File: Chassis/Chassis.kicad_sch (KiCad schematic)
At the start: 4 parts

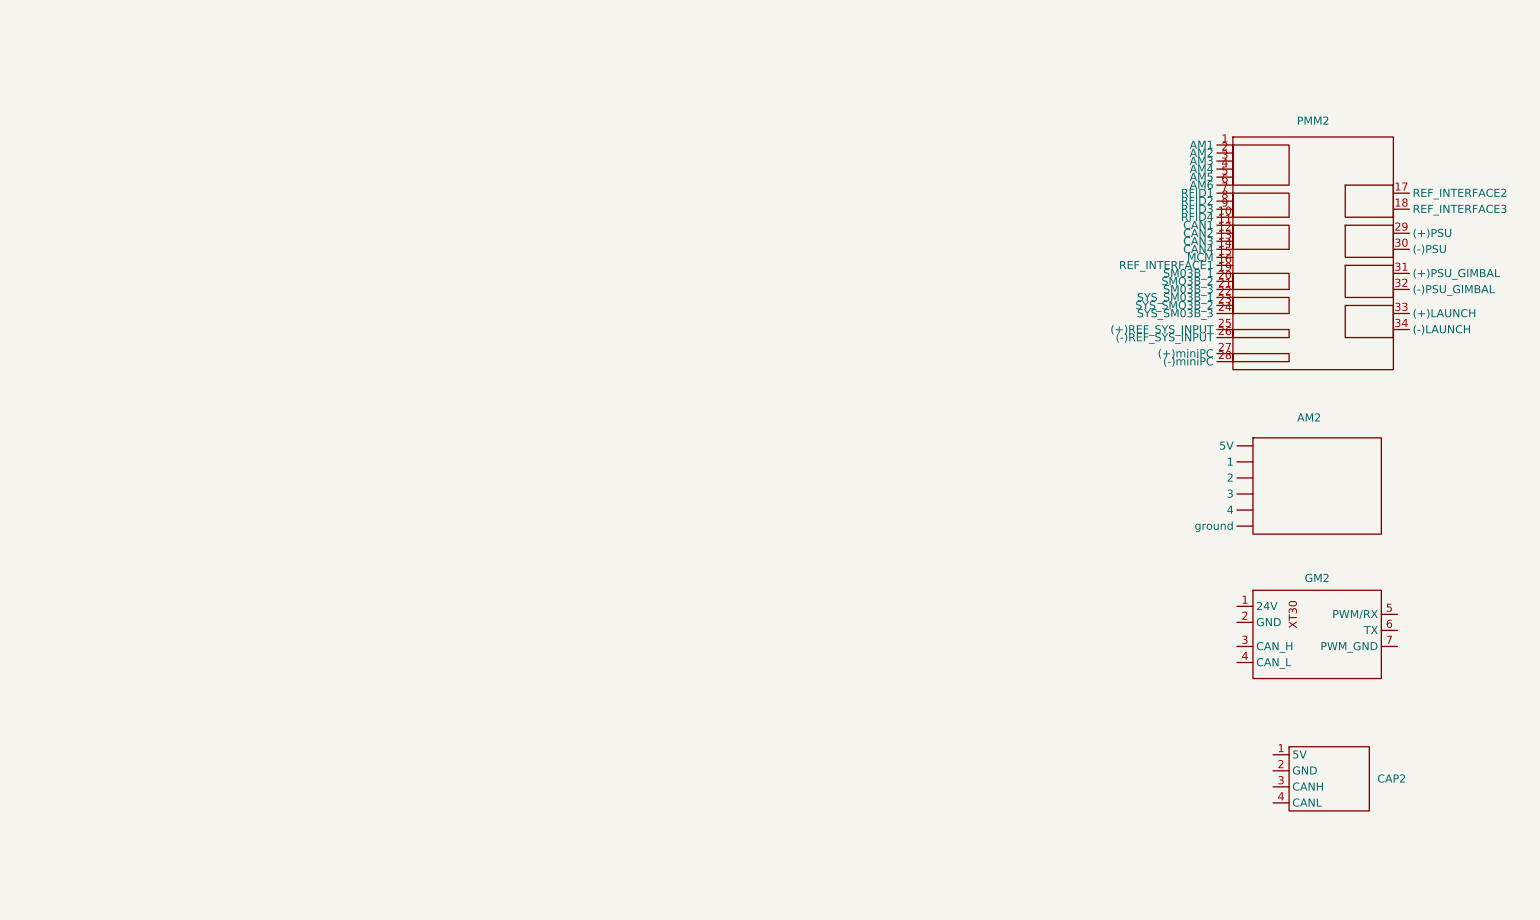
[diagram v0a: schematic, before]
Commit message: Reorganized chassis, turret, devboard shield, into monorepo
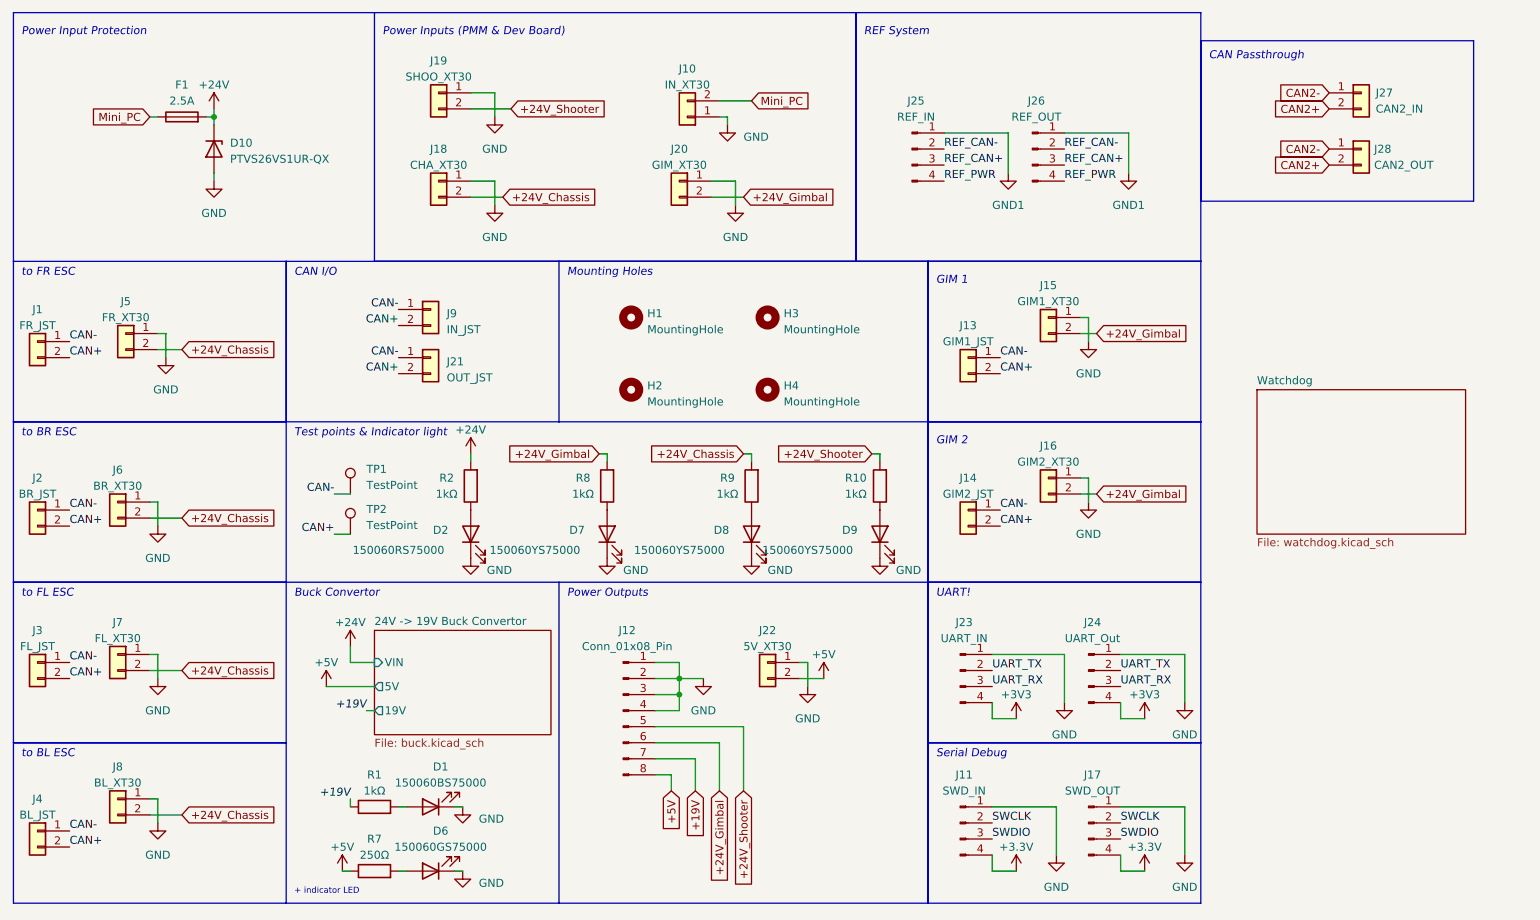
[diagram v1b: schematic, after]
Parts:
- removed AM2: ~, symbol Robomaster_Library:AM
- removed CAP2: ~, symbol Robomaster_Library:CAP
- removed GM2: ~, symbol Robomaster_Library:GM6020
- removed PMM2: ~, symbol Robomaster_Library:PMM
- added D1: 150060BS75000, LED_SMD:LED_0603_1608Metric_Pad1.05x0.95mm_HandSolder, symbol Device:LED
- added D10: PTVS26VS1UR-QX, Robomaster_Passives:PTVS26VS1URQX, symbol Device:D_Zener
- added D2: 150060RS75000, LED_SMD:LED_0603_1608Metric_Pad1.05x0.95mm_HandSolder, symbol Device:LED
- added D6: 150060GS75000, LED_SMD:LED_0603_1608Metric_Pad1.05x0.95mm_HandSolder, symbol Device:LED
- added D7, D8, D9: 150060YS75000, LED_SMD:LED_0603_1608Metric_Pad1.05x0.95mm_HandSolder, symbol Device:LED
- added F1: 2.5A, Fuse:Fuse_0603_1608Metric_Pad1.05x0.95mm_HandSolder, symbol Device:Fuse
- added H1, H2, H3, H4: MountingHole, MountingHole:MountingHole_3.2mm_M3, symbol Mechanical:MountingHole
- added J1: FR_JST, Connector_JST:JST_GH_BM02B-GHS-TBT_1x02-1MP_P1.25mm_Vertical, symbol Connector_Generic:Conn_01x02
- added J10: IN_XT30, Robomaster_Connectors:AMASS_XT30U-F_1x02_P5.0mm_Vertical, symbol Connector_Generic:Conn_01x02
- added J11: SWD_IN, Connector_JST:JST_GH_BM04B-GHS-TBT_1x04-1MP_P1.25mm_Vertical, symbol Connector:Conn_01x04_Pin
- added J12: Conn_01x08_Pin, Robomaster_Connectors:CON_1722981108_MOL, symbol Connector:Conn_01x08_Pin
- added J13: GIM1_JST, Connector_JST:JST_GH_BM02B-GHS-TBT_1x02-1MP_P1.25mm_Vertical, symbol Connector_Generic:Conn_01x02
- added J14: GIM2_JST, Connector_JST:JST_GH_BM02B-GHS-TBT_1x02-1MP_P1.25mm_Vertical, symbol Connector_Generic:Conn_01x02
- added J15: GIM1_XT30, Robomaster_Connectors:AMASS_XT30U-F_1x02_P5.0mm_Vertical, symbol Connector_Generic:Conn_01x02
- added J16: GIM2_XT30, Robomaster_Connectors:AMASS_XT30U-F_1x02_P5.0mm_Vertical, symbol Connector_Generic:Conn_01x02
- added J17: SWD_OUT, Connector_JST:JST_GH_BM04B-GHS-TBT_1x04-1MP_P1.25mm_Vertical, symbol Connector:Conn_01x04_Pin
- added J18: CHA_XT30, Robomaster_Connectors:AMASS_XT30U-F_1x02_P5.0mm_Vertical, symbol Connector_Generic:Conn_01x02
- added J19: SHOO_XT30, Robomaster_Connectors:AMASS_XT30U-F_1x02_P5.0mm_Vertical, symbol Connector_Generic:Conn_01x02
- added J2: BR_JST, Connector_JST:JST_GH_BM02B-GHS-TBT_1x02-1MP_P1.25mm_Vertical, symbol Connector_Generic:Conn_01x02
- added J20: GIM_XT30, Robomaster_Connectors:AMASS_XT30U-F_1x02_P5.0mm_Vertical, symbol Connector_Generic:Conn_01x02
- added J21: OUT_JST, Connector_JST:JST_GH_BM02B-GHS-TBT_1x02-1MP_P1.25mm_Vertical, symbol Connector_Generic:Conn_01x02
- added J22: 5V_XT30, Robomaster_Connectors:AMASS_XT30U-F_1x02_P5.0mm_Vertical, symbol Connector_Generic:Conn_01x02
- added J23: UART_IN, Connector_JST:JST_GH_BM04B-GHS-TBT_1x04-1MP_P1.25mm_Vertical, symbol Connector:Conn_01x04_Pin
- added J24: UART_Out, Connector_JST:JST_GH_BM04B-GHS-TBT_1x04-1MP_P1.25mm_Vertical, symbol Connector:Conn_01x04_Pin
- added J25: REF_IN, Connector_JST:JST_GH_BM04B-GHS-TBT_1x04-1MP_P1.25mm_Vertical, symbol Connector:Conn_01x04_Pin
- added J26: REF_OUT, Connector_JST:JST_GH_BM04B-GHS-TBT_1x04-1MP_P1.25mm_Vertical, symbol Connector:Conn_01x04_Pin
- added J27: CAN2_IN, Connector_JST:JST_GH_BM02B-GHS-TBT_1x02-1MP_P1.25mm_Vertical, symbol Connector_Generic:Conn_01x02
- added J28: CAN2_OUT, Connector_JST:JST_GH_BM02B-GHS-TBT_1x02-1MP_P1.25mm_Vertical, symbol Connector_Generic:Conn_01x02
- added J3: FL_JST, Connector_JST:JST_GH_BM02B-GHS-TBT_1x02-1MP_P1.25mm_Vertical, symbol Connector_Generic:Conn_01x02
- added J4: BL_JST, Connector_JST:JST_GH_BM02B-GHS-TBT_1x02-1MP_P1.25mm_Vertical, symbol Connector_Generic:Conn_01x02
- added J5: FR_XT30, Robomaster_Connectors:AMASS_XT30U-F_1x02_P5.0mm_Vertical, symbol Connector_Generic:Conn_01x02
- added J6: BR_XT30, Robomaster_Connectors:AMASS_XT30U-F_1x02_P5.0mm_Vertical, symbol Connector_Generic:Conn_01x02
- added J7: FL_XT30, Robomaster_Connectors:AMASS_XT30U-F_1x02_P5.0mm_Vertical, symbol Connector_Generic:Conn_01x02
- added J8: BL_XT30, Robomaster_Connectors:AMASS_XT30U-F_1x02_P5.0mm_Vertical, symbol Connector_Generic:Conn_01x02
- added J9: IN_JST, Connector_JST:JST_GH_BM02B-GHS-TBT_1x02-1MP_P1.25mm_Vertical, symbol Connector_Generic:Conn_01x02
- added R1, R10, R2, R8, R9: 1kΩ, Resistor_SMD:R_0603_1608Metric_Pad0.98x0.95mm_HandSolder, symbol Device:R
- added R7: 250Ω, Resistor_SMD:R_0603_1608Metric_Pad0.98x0.95mm_HandSolder, symbol Device:R
- added TP1, TP2: TestPoint, TestPoint:TestPoint_Pad_2.0x2.0mm, symbol Connector:TestPoint
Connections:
- new net: D6.2 (A), R7.2
- new net: D9.2 (A), R10.1
- new net: D7.2 (A), R8.1
- new net: D2.2 (A), R2.1
- new net: D8.2 (A), R9.1
- new net: D1.2 (A), R1.2
- new net +19V: J12.7 (Pin_7), R1.1
- new net +24V: D10.1 (K), F1.2, R2.2
- new net +24V_Chassis: J18.2 (Pin_2), J5.2 (Pin_2), J6.2 (Pin_2), J7.2 (Pin_2), J8.2 (Pin_2), R9.2
- new net +24V_Gimbal: J12.6 (Pin_6), J15.2 (Pin_2), J16.2 (Pin_2), J20.2 (Pin_2), R8.2
- new net +24V_Shooter: J12.5 (Pin_5), J19.2 (Pin_2), R10.2
- new net +3.3V: J11.4 (Pin_4), J17.4 (Pin_4)
- new net +3V3: J23.4 (Pin_4), J24.4 (Pin_4)
- new net +5V: J12.8 (Pin_8), J22.2 (Pin_2), R7.1
- new net CAN+: J1.2 (Pin_2), J13.2 (Pin_2), J14.2 (Pin_2), J2.2 (Pin_2), J21.2 (Pin_2), J3.2 (Pin_2), J4.2 (Pin_2), J9.2 (Pin_2), TP2.1
- new net CAN-: J1.1 (Pin_1), J13.1 (Pin_1), J14.1 (Pin_1), J2.1 (Pin_1), J21.1 (Pin_1), J3.1 (Pin_1), J4.1 (Pin_1), J9.1 (Pin_1), TP1.1
- new net CAN2+: J27.2 (Pin_2), J28.2 (Pin_2)
- new net CAN2-: J27.1 (Pin_1), J28.1 (Pin_1)
- new net GND: D1.1 (K), D10.2 (A), D2.1 (K), D6.1 (K), D7.1 (K), D8.1 (K), D9.1 (K), J10.1 (Pin_1), J11.1 (Pin_1), J12.1 (Pin_1), J12.2 (Pin_2), J12.3 (Pin_3), J12.4 (Pin_4), J15.1 (Pin_1), J16.1 (Pin_1), J17.1 (Pin_1), J18.1 (Pin_1), J19.1 (Pin_1), J20.1 (Pin_1), J22.1 (Pin_1), J23.1 (Pin_1), J24.1 (Pin_1), J5.1 (Pin_1), J6.1 (Pin_1), J7.1 (Pin_1), J8.1 (Pin_1)
- new net GND1: J25.1 (Pin_1), J26.1 (Pin_1)
- new net Mini_PC: F1.1, J10.2 (Pin_2)
- new net REF_CAN+: J25.3 (Pin_3), J26.3 (Pin_3)
- new net REF_CAN-: J25.2 (Pin_2), J26.2 (Pin_2)
- new net REF_PWR: J25.4 (Pin_4), J26.4 (Pin_4)
- new net SWCLK: J11.2 (Pin_2), J17.2 (Pin_2)
- new net SWDIO: J11.3 (Pin_3), J17.3 (Pin_3)
- new net UART_RX: J23.3 (Pin_3), J24.3 (Pin_3)
- new net UART_TX: J23.2 (Pin_2), J24.2 (Pin_2)
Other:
- added sheet 24V -> 19V Buck Convertor (buck.kicad_sch)
- added sheet Watchdog (watchdog.kicad_sch)
- note added: "+ indicator LED"
- note added: "Buck Convertor"
- note added: "CAN I/O"
- note added: "CAN Passthrough"
- note added: "GIM 1"
- note added: "GIM 2"
- note added: "Mounting Holes"
- note added: "Power Input Protection"
- note added: "Power Inputs (PMM & Dev Board)"
- note added: "Power Outputs"
- note added: "REF System"
- note added: "Serial Debug"
- note added: "Test points & Indicator light"
- note added: "UART!"
- note added: "to BL ESC"
- note added: "to BR ESC"
- note added: "to FL ESC"
- note added: "to FR ESC"
- company: (none) -> UT RoboMasters
- title: (none) -> Chassis
